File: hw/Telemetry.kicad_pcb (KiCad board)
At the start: 4 copper layers, 100 x 82 mm, 105 parts, among them J101 VS1053 EXP, J102 BOOT0, J103 SPORT, J104 SBUS, J105 USB_B_Micro, J106 UART_EXP, J201 Conn_01x02, J301 Conn_01x02, J302 Conn_01x02, J401 Conn_01x02, J402 Conn_01x02, J403 Conn_01x02, J404 Conn_01x02, J405 Conn_01x02, J406 Conn_01x02, J407 Conn_01x02, J408 Conn_01x02, J409 SERVO_OUT, Q201 AO3401A, Q202 AO3401A, Q203 IRLML6344TRPBF, Q204 IRLML6344TRPBF, Q401 IRLML6344TRPBF, Q402 IRLML6344TRPBF, Q403 IRLML6344TRPBF, Q404 IRLZ44N, Q405 IRLML6344TRPBF, Q406 IRLML6344TRPBF, Q407 IRLML6344TRPBF, Q408 IRLZ44N, SW101 SW_Push, U101 STM32F303CBx, U201 AP1501-K5, U202 RT6200, U301 LP2985-5.0, U302 ACS770xCB-100U-PSF, U303 OP179GRT, U304 ACS770xCB-100U-PSF, U305 OP179GRT, X101 TXC-7C

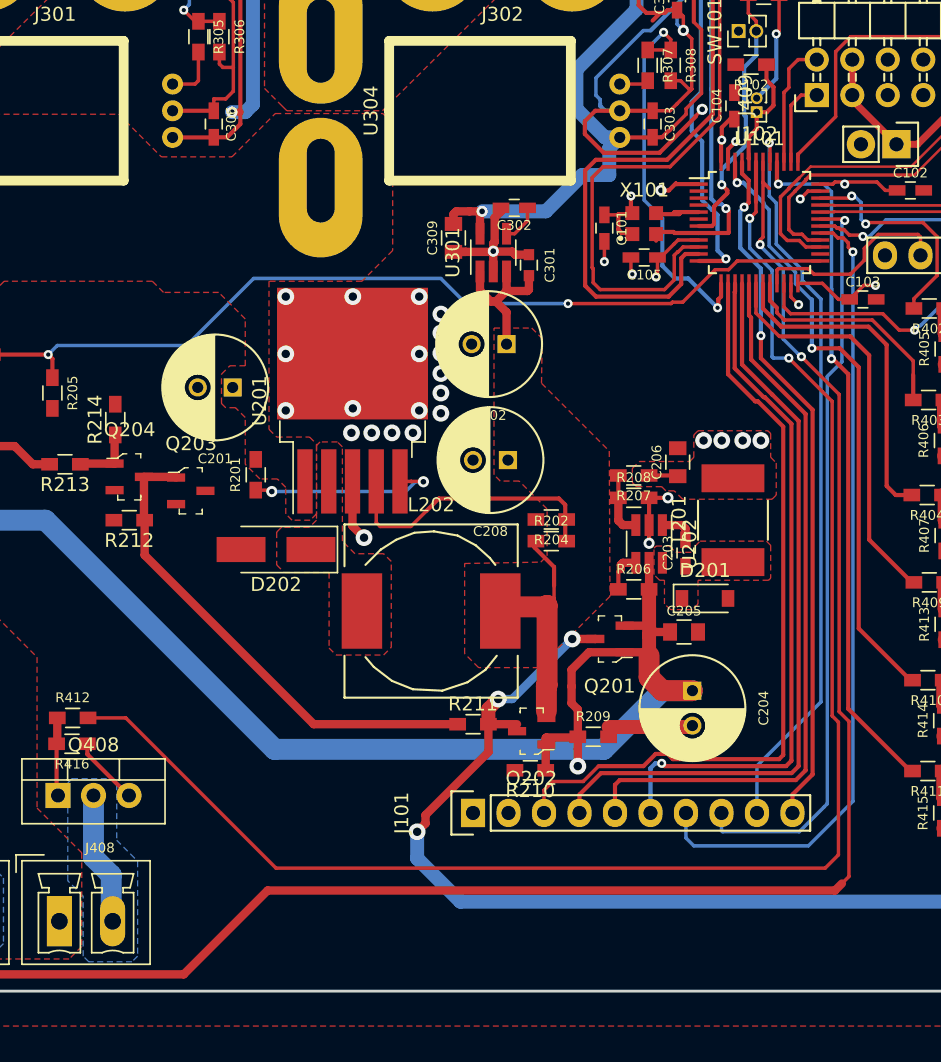
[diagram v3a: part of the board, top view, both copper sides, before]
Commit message: Fixed crash problems
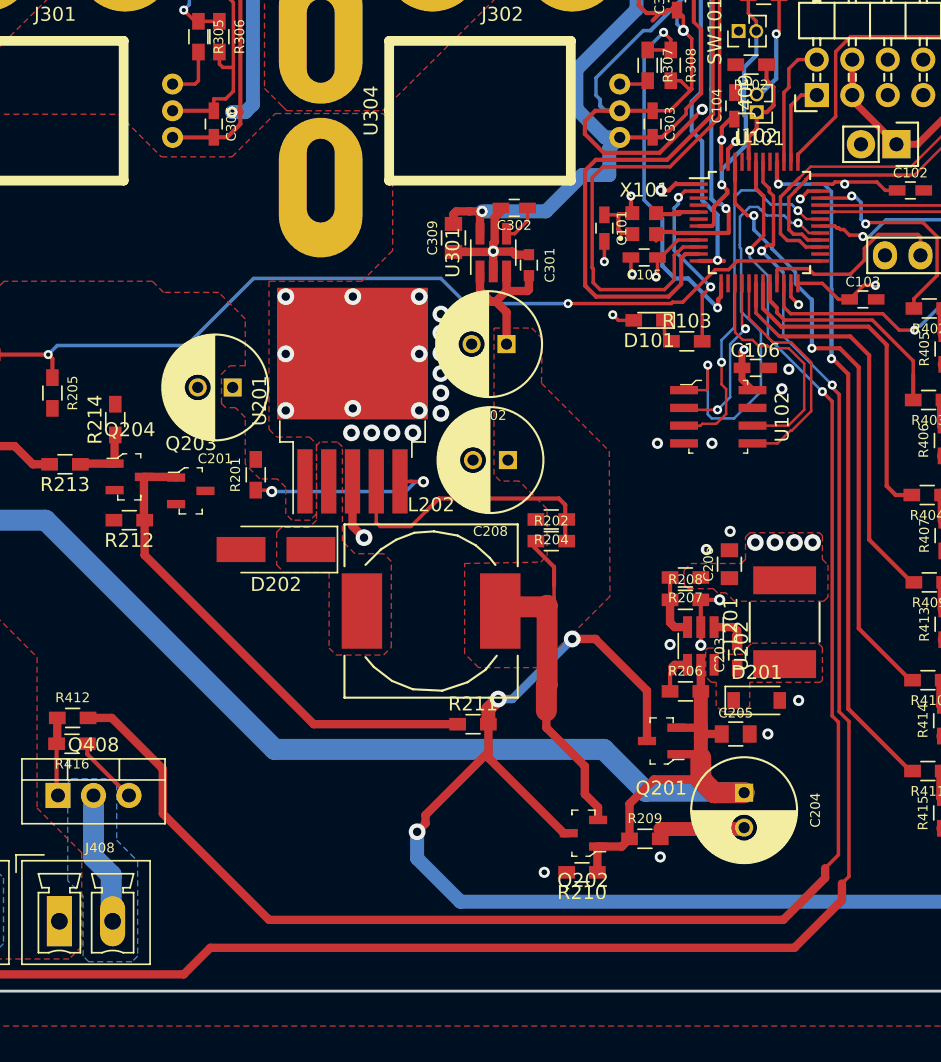
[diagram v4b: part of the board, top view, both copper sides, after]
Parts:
- removed J101: VS1053 EXP, Pin_Headers:Pin_Header_Straight_1x10
- added C106: 100n, Capacitors_SMD:C_0603_HandSoldering, F.Cu at (128.2, 75.4)
- added D101: LED, LEDs:LED_0603_HandSoldering, F.Cu at (120.6, 72.0)
- added R103: 470R, Resistors_SMD:R_0603_HandSoldering, F.Cu at (123.3, 73.5)
- added U102: IS25LP032D, digikey-footprints:SOIC-8_W3.9mm, F.Cu at (125.5, 78.9)
- J102: footprint Pin_Headers:Pin_Header_Straight_1x02_Pitch1.00mm -> Pin_Headers:Pin_Header_Straight_1x02_Pitch1.27mm
- moved R207 8.18 mm to (123.2, 90.4)
- moved D201 8.18 mm to (128.3, 99.2)
- moved L201 8.18 mm to (130.3, 93.6)
- moved C203 8.18 mm to (126.9, 96.0)
- moved C204 8.18 mm to (127.4, 105.8)
- moved C205 8.18 mm to (126.8, 101.6)
- moved Q201 8.18 mm to (121.5, 102.1)
- moved Q202 8.18 mm to (115.9, 108.7)
- moved R206 8.18 mm to (123.2, 98.5)
- moved R208 8.18 mm to (123.2, 92.0)
- moved R209 8.18 mm to (120.3, 109.1)
- moved R210 8.18 mm to (115.8, 111.5)
- moved U202 8.18 mm to (124.3, 95.3)
- moved C206 8.18 mm to (126.3, 89.5)
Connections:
- U101 pad 14: /SPI_CS -> (no net)
- U101 pad 2: (no net) -> Net-(R103-Pad2)
- U101 pad 29: /XCS -> /SPI_CS
- U101 pad 31: /XRESET -> /WP
- U101 pad 41: /XDCS -> (no net)
- U101 pad 45: /DREQ -> (no net)
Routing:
- net /XCS: track 57.7 -> 0.00 mm, vias 1 -> 0
- net /XRESET: track 53.8 -> 0.00 mm, vias 1 -> 0
- net /XDCS: track 52.8 -> 0.00 mm, vias 1 -> 0
- net /DREQ: track 49.8 -> 0.00 mm, vias 2 -> 0
- net /SPI_MISO: track 54.1 -> 12.4 mm, vias 0 -> 2
- net /SPI_MOSI: track 52.6 -> 16.9 mm
- net /SPI_SCK: track 49.6 -> 16.9 mm, vias 1 -> 0
- net /WP: track 0.00 -> 26.6 mm, vias 0 -> 2
- net /SPI_CS: track 55.6 -> 31.6 mm, vias 0 -> 2
- net VBUS: track 136.0 -> 151.2 mm
- net Net-(R103-Pad2): track 0.00 -> 13.4 mm, vias 0 -> 2
- net VCC: track 27.8 -> 37.1 mm
- net HC_OUT2: track 111.6 -> 116.8 mm
- net +3V3: track 39.6 -> 42.4 mm, vias 11 -> 13
- net Net-(D101-Pad1): track 0.00 -> 1.71 mm
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
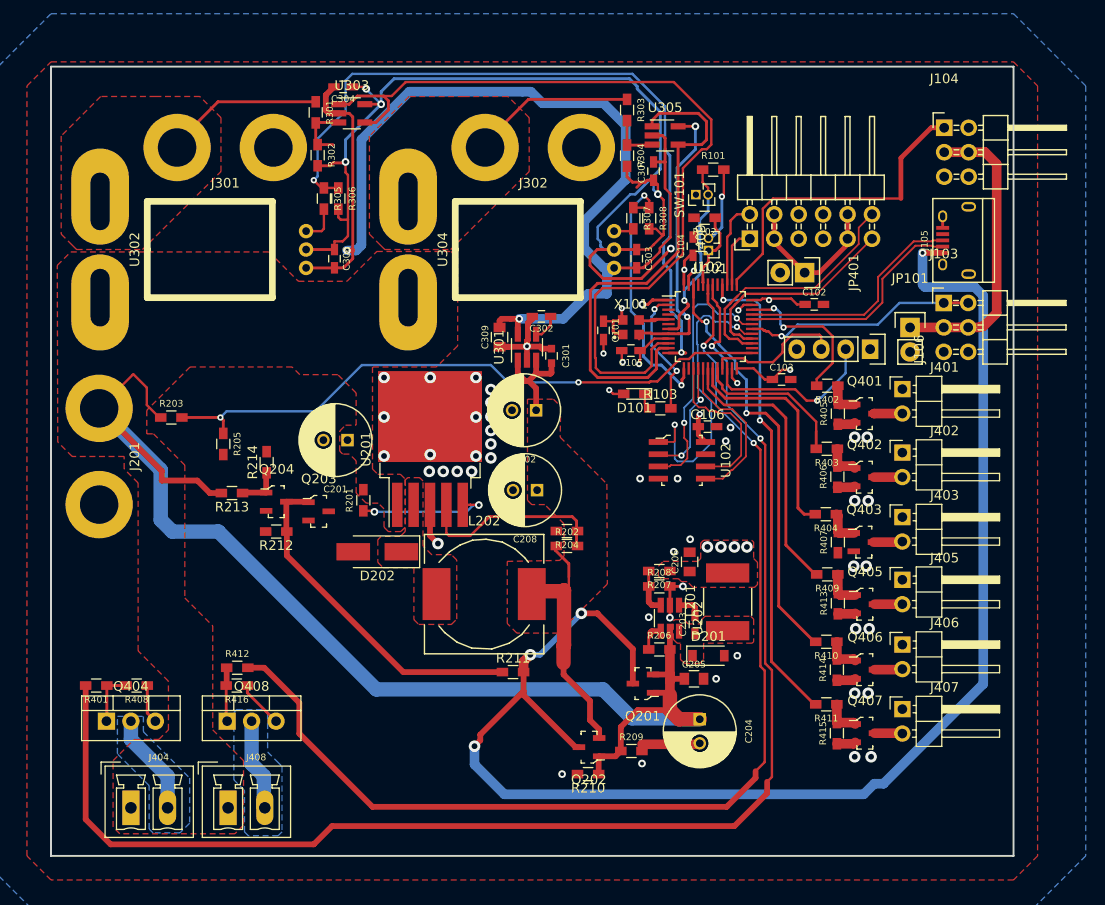
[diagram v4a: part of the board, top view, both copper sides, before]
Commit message: Switched High Current FETs and added drivers for those
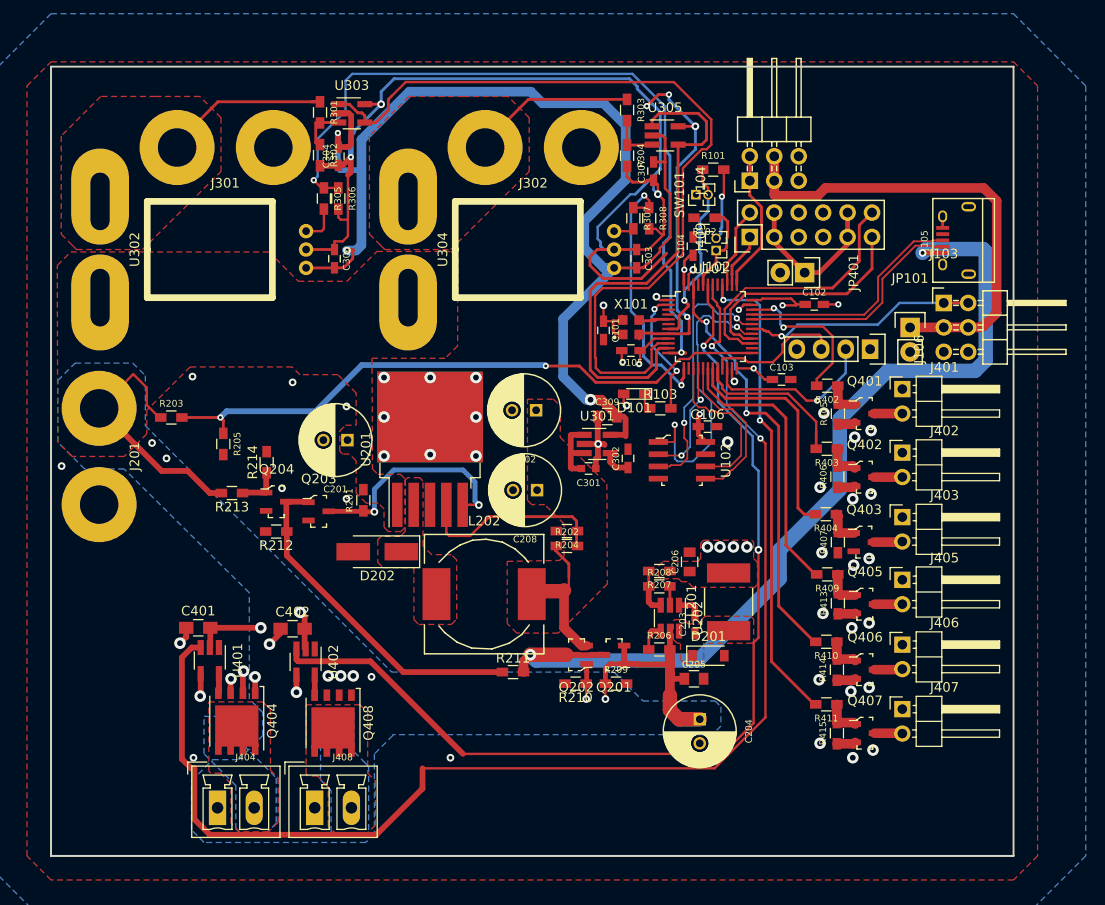
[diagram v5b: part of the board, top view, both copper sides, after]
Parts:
- removed R401, R412: 10, Resistors_SMD:R_0603_HandSoldering
- removed R408, R416: 10k, Resistors_SMD:R_0603_HandSoldering
- added C401: 1u, Capacitors_SMD:C_0805_HandSoldering, F.Cu at (75.3, 96.3)
- added C402: 1u, Capacitors_SMD:C_0805_HandSoldering, F.Cu at (85.1, 96.4)
- added U401: MCP1416, TO_SOT_Packages_SMD:SOT-23-5_HandSoldering, F.Cu at (76.5, 99.7)
- added U402: MCP1416, TO_SOT_Packages_SMD:SOT-23-5_HandSoldering, F.Cu at (86.5, 99.8)
- J409: footprint Pin_Headers:Pin_Header_Angled_2x06 -> Pin_Headers:Pin_Header_Straight_2x06
- Q404, Q408: value IRLZ44N -> CSD17306Q5A; footprint TO_SOT_Packages_THT:TO-220_Vertical -> TO_SOT_Packages_SMD:TDSON-8-1_HandSoldering
- moved J104 20.9 mm to (132.6, 49.9), turned to 90 degrees
- moved C302 17.3 mm to (120.0, 78.7), turned to 90 degrees
- moved C309 13.9 mm to (117.8, 74.3), turned to 0 degrees
- moved Q404 13.5 mm to (79.3, 106.0), turned to 270 degrees
- moved U301 12.4 mm to (116.8, 77.2), turned to 0 degrees
- moved C301 12.3 mm to (115.8, 79.8), turned to 180 degrees
- moved Q408 11.0 mm to (89.3, 106.2), turned to 270 degrees
- moved Q202 9.69 mm to (114.6, 99.1)
- moved R210 9.49 mm to (114.5, 102.1)
- moved J404 9.00 mm to (77.3, 115.0)
- moved J408 9.00 mm to (87.4, 115.0)
- moved C304 7.22 mm to (89.8, 47.3), turned to 90 degrees
- moved R209 7.18 mm to (118.7, 102.1)
- moved Q201 4.24 mm to (118.5, 99.1)
- moved J102 0.80 mm to (129.1, 57.1)
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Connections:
- Q404 pad 1: Net-(Q404-Pad1) -> GND
- Q404 pad 2: Net-(J404-Pad2) -> GND
- Q408 pad 1: Net-(Q408-Pad1) -> GND
- Q408 pad 2: Net-(J408-Pad2) -> GND
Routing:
- net +BATT: track 136.3 -> 70.3 mm, vias 0 -> 4
- net VBUS: track 151.2 -> 96.5 mm, vias 4 -> 2
- net /Sbus: track 33.8 -> 15.4 mm
- net Net-(J103-Pad3): track 31.1 -> 49.3 mm
- net HC_OUT2: track 116.8 -> 102.7 mm
- net VCC: track 37.1 -> 23.2 mm
- net Net-(J404-Pad2): track 10.6 -> 0.00 mm
- net Net-(J408-Pad2): track 9.53 -> 0.00 mm
- net HC_OUT1: track 144.6 -> 135.1 mm
- net Net-(Q203-Pad3): track 14.1 -> 23.2 mm
- net GND: track 203.1 -> 196.1 mm, vias 57 -> 61
- net Net-(Q404-Pad1): track 5.72 -> 0.00 mm
- net Net-(Q408-Pad1): track 5.61 -> 0.00 mm
- net +3V3: track 42.4 -> 39.9 mm
- net Net-(Q408-Pad4): track 0.00 -> 2.10 mm
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- added copper zone on B.Cu, net +BATT
- added copper zone on F.Cu, net Net-(J404-Pad2)
- added copper zone on F.Cu, net Net-(J408-Pad2)

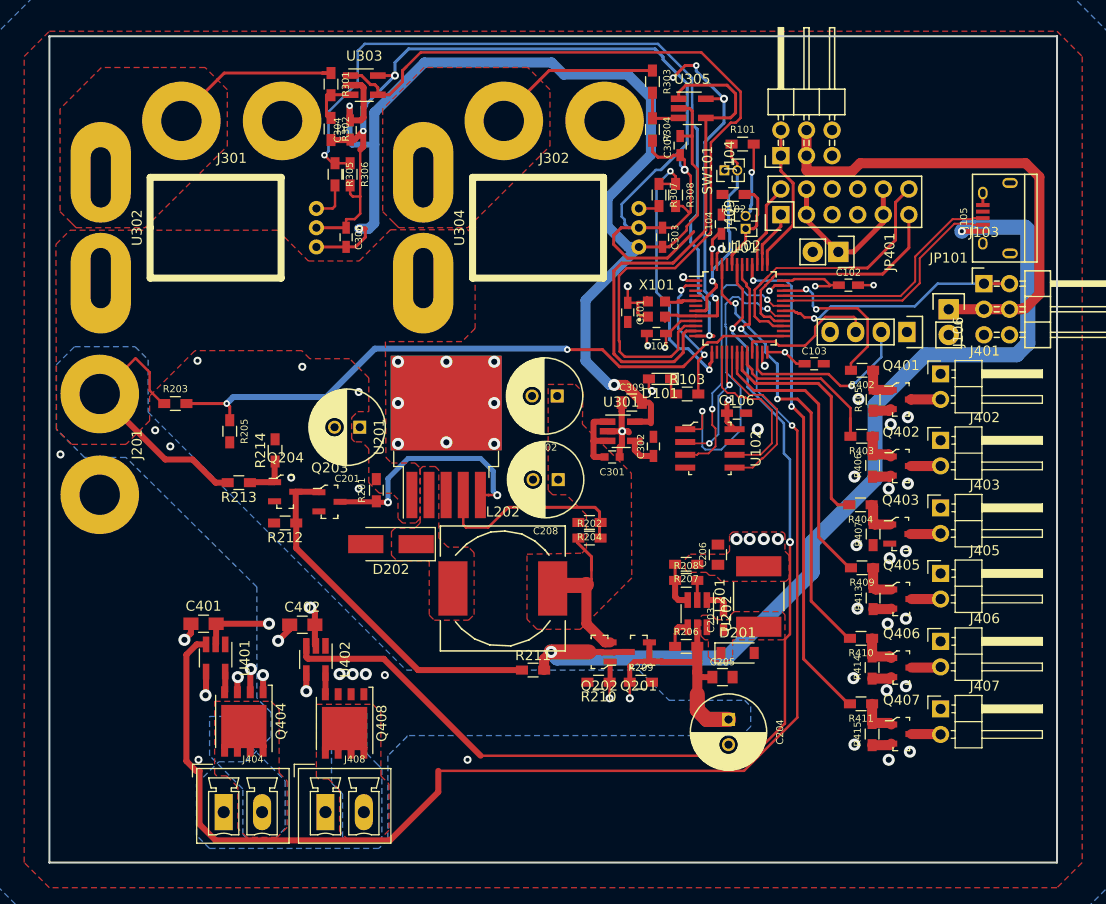
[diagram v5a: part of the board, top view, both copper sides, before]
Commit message: Added DAC output connector to the design
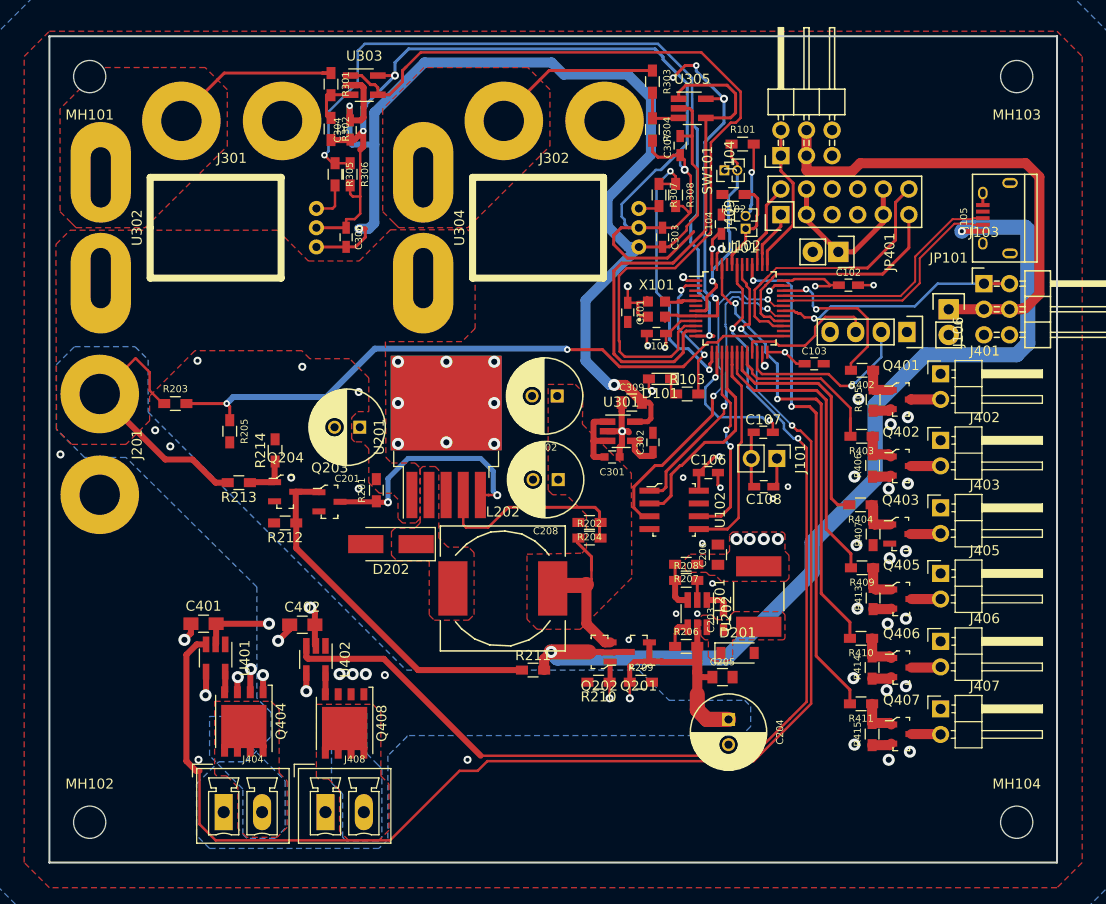
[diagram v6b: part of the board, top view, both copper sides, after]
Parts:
- added C107: 10u, Capacitors_SMD:C_0603_HandSoldering, F.Cu at (130.8, 77.3)
- added C108: 10p, Capacitors_SMD:C_0603_HandSoldering, F.Cu at (130.9, 82.7)
- added J101: AUDIO, Pin_Headers:Pin_Header_Straight_1x02_Pitch2.54mm, F.Cu at (132.2, 79.9)
- added MH101: MountingHole, Mounting_Holes:MountingHole_3.2mm_M3_DIN965, F.Cu at (64.0, 42.0)
- added MH102: MountingHole, Mounting_Holes:MountingHole_3.2mm_M3_DIN965, F.Cu at (64.0, 116.0)
- added MH103: MountingHole, Mounting_Holes:MountingHole_3.2mm_M3_DIN965, F.Cu at (156.0, 42.0)
- added MH104: MountingHole, Mounting_Holes:MountingHole_3.2mm_M3_DIN965, F.Cu at (156.0, 116.0)
- moved U102 7.06 mm to (122.0, 85.0)
- moved C106 6.53 mm to (125.4, 81.3)
- moved C302 0.40 mm to (119.9, 78.3)
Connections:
- U101 pad 14: (no net) -> Net-(C107-Pad2)
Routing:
- net Net-(C107-Pad2): track 0.00 -> 14.0 mm, vias 0 -> 2
- net /SPI_MISO: track 12.4 -> 20.9 mm, vias 2 -> 0
- net /WP: track 26.6 -> 33.7 mm
- net Net-(C107-Pad1): track 0.00 -> 5.62 mm
- net GND: track 196.1 -> 200.6 mm, vias 61 -> 69
- net /SPI_MOSI: track 16.9 -> 21.4 mm
- net /SPI_SCK: track 16.9 -> 19.6 mm, vias 0 -> 2
- net /SPI_CS: track 31.6 -> 29.3 mm
- net HC_OUT2: track 102.7 -> 104.4 mm
- net +3V3: track 39.9 -> 41.2 mm
- net OUT4: track 43.9 -> 44.9 mm
- net OUT6: track 49.7 -> 50.6 mm
- net OUT2: track 29.1 -> 29.7 mm

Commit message: Lots and lots of updates Added DAC amplifier that can be controlled Cleaned up the schematic
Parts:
- removed C107: 10u, Capacitors_SMD:C_0603_HandSoldering
- removed C108: 10p, Capacitors_SMD:C_0603_HandSoldering
- removed J101: AUDIO, Pin_Headers:Pin_Header_Straight_1x02_Pitch2.54mm
- added C403: 100n, Capacitors_SMD:C_0603_HandSoldering, F.Cu at (128.2, 87.8)
- added C404: 10u, Capacitors_SMD:C_0603_HandSoldering, F.Cu at (119.2, 88.3)
- added C405: 100n, Capacitors_SMD:C_0603_HandSoldering, F.Cu at (121.9, 84.5)
- added C406: 100n, Capacitors_SMD:C_0603_HandSoldering, F.Cu at (128.2, 91.9)
- added J410: AUDIO, Pin_Headers:Pin_Header_Straight_1x02_Pitch2.54mm, F.Cu at (119.2, 82.0)
- added R401: 10k, Resistors_SMD:R_0603_HandSoldering, F.Cu at (120.0, 91.0)
- added R408: 10k, Resistors_SMD:R_0603_HandSoldering, F.Cu at (125.1, 84.8)
- added U403: MCP4012-xxxxCH, TO_SOT_Packages_SMD:SOT-23-6_Handsoldering, F.Cu at (124.8, 91.9)
- added U404: OP179GRT, TO_SOT_Packages_SMD:SOT-23-5_HandSoldering, F.Cu at (123.8, 88.1)
- L201: footprint Inductors_NEOSID:Neosid_Inductor_SM-NE56_SMD2220 -> Inductors:Inductor_Taiyo-Yuden_MD-3030
- L202: footprint Inductors_NEOSID:Neosid_Inductor_SM-NE127 -> PCBDecals:12x12_inductor
- moved C204 12.6 mm to (114.8, 105.5), turned to 0 degrees
- moved Q201 11.4 mm to (109.0, 105.4)
- moved Q202 11.4 mm to (105.1, 105.4)
- moved R209 11.4 mm to (109.2, 108.4)
- moved R210 11.4 mm to (105.0, 108.4)
- moved U102 10.6 mm to (131.9, 81.1), turned to 0 degrees
- moved R211 8.49 mm to (100.8, 105.4)
- moved L201 7.64 mm to (128.5, 101.0)
- moved R204 6.95 mm to (106.8, 87.9)
- moved R206 6.66 mm to (122.3, 105.2)
- moved C205 6.66 mm to (125.9, 108.2)
- moved U202 6.66 mm to (123.4, 101.9)
- moved D201 6.66 mm to (127.4, 105.8)
- moved R207 6.66 mm to (122.3, 97.0)
- moved R208 6.66 mm to (122.3, 98.6)
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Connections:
- U101 pad 14: Net-(C107-Pad2) -> DAC_OUT
- U101 pad 3: (no net) -> AMP_DIR
- U101 pad 4: (no net) -> AMP_CS
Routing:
- net +5VA: track 127.9 -> 169.4 mm, vias 3 -> 5
- net AMP_CS: track 0.00 -> 33.9 mm, vias 0 -> 2
- net AMP_DIR: track 0.00 -> 33.8 mm, vias 0 -> 2
- net VBUS: track 96.5 -> 124.4 mm
- net DAC_OUT: track 0.00 -> 26.0 mm, vias 0 -> 2
- net GND: track 200.6 -> 182.7 mm, vias 69 -> 78
- net HC_OUT2: track 104.4 -> 122.0 mm
- net Net-(C107-Pad2): track 14.0 -> 0.00 mm, vias 2 -> 0
- net Net-(C405-Pad2): track 0.00 -> 13.8 mm, vias 0 -> 2
- net /SPI_MOSI: track 21.4 -> 12.5 mm
- net Net-(C404-Pad2): track 0.00 -> 8.34 mm
- net VCC: track 23.2 -> 30.4 mm, vias 0 -> 8
- net /SPI_SCK: track 19.6 -> 12.9 mm
- net Net-(R202-Pad2): track 19.9 -> 13.8 mm
- net Net-(C107-Pad1): track 5.62 -> 0.00 mm
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- removed copper zone on B.Cu, net Net-(J404-Pad2)
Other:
- rule pad_to_mask_clearance: 0.2 -> 0.18
